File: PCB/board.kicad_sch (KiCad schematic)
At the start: 171 parts, among them J1 Micro_SD_Card, J10 Conn_01x10, J11 Conn_01x02, J12 Conn_02x04_Odd_Even, J13 Conn_01x02, J14 Conn_01x02, J15 Conn_01x03, J16 Conn_01x02, J17 Conn_01x05, J18 Conn_01x04, J19 Conn_01x04, J2 Conn_ARM_JTAG_SWD_10, J20 Conn_01x02, J21 Conn_01x03, J22 Conn_02x04_Odd_Even, J23 Conn_01x04, J24 Conn_01x04, J25 Conn_01x02, J26 Conn_01x03, J27 Conn_02x04_Odd_Even, J28 Conn_01x04, J29 Conn_01x04, J30 Conn_01x02, J31 Conn_01x03, J32 Conn_01x02, J33 Conn_01x02, J34 Conn_01x02, J35 Conn_01x02, J36 Conn_01x02, J37 Conn_01x02, J4 Conn_01x04, J5 Conn_01x04, J6 Conn_01x02, J7 Conn_01x03, J8 Conn_02x04_Odd_Even, J9 Conn_01x10, P1 USB_C_Plug_USB2.0, Q1 IRLML6402, Q2 NMOS, Q3 NMOS, Q4 NMOS, Q5 NMOS, Q6 NMOS, SW1 SW_SPST, SW2 SW_Push, U1 STM32H743VITx, U2 AMS1117-3.3, U3 TPS54331, U4 TMC2209_SILENTSTEPSTICK, U5 TMC2209_SILENTSTEPSTICK, U6 TMC2209_SILENTSTEPSTICK, U7 TMC2209_SILENTSTEPSTICK, Y1 25 MHz

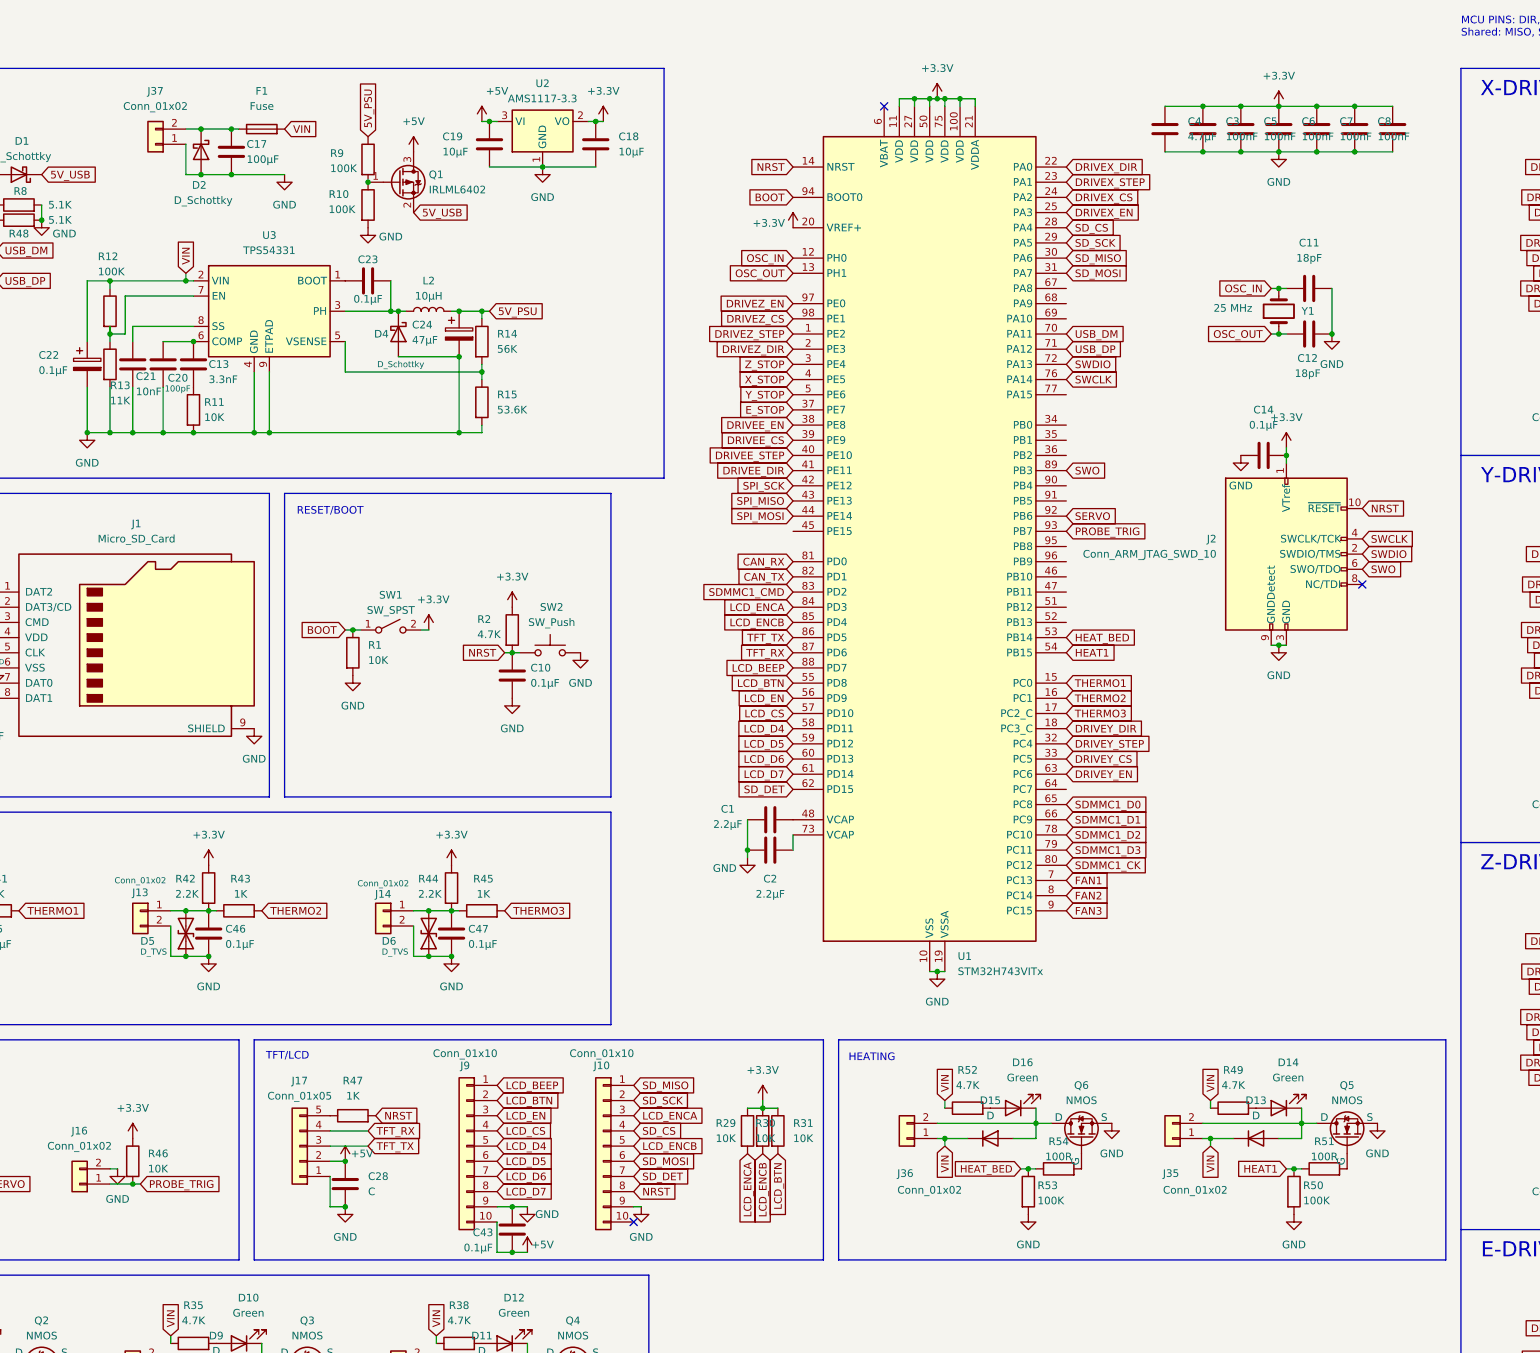
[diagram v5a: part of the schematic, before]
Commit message: most of the capacitors using assign footprints
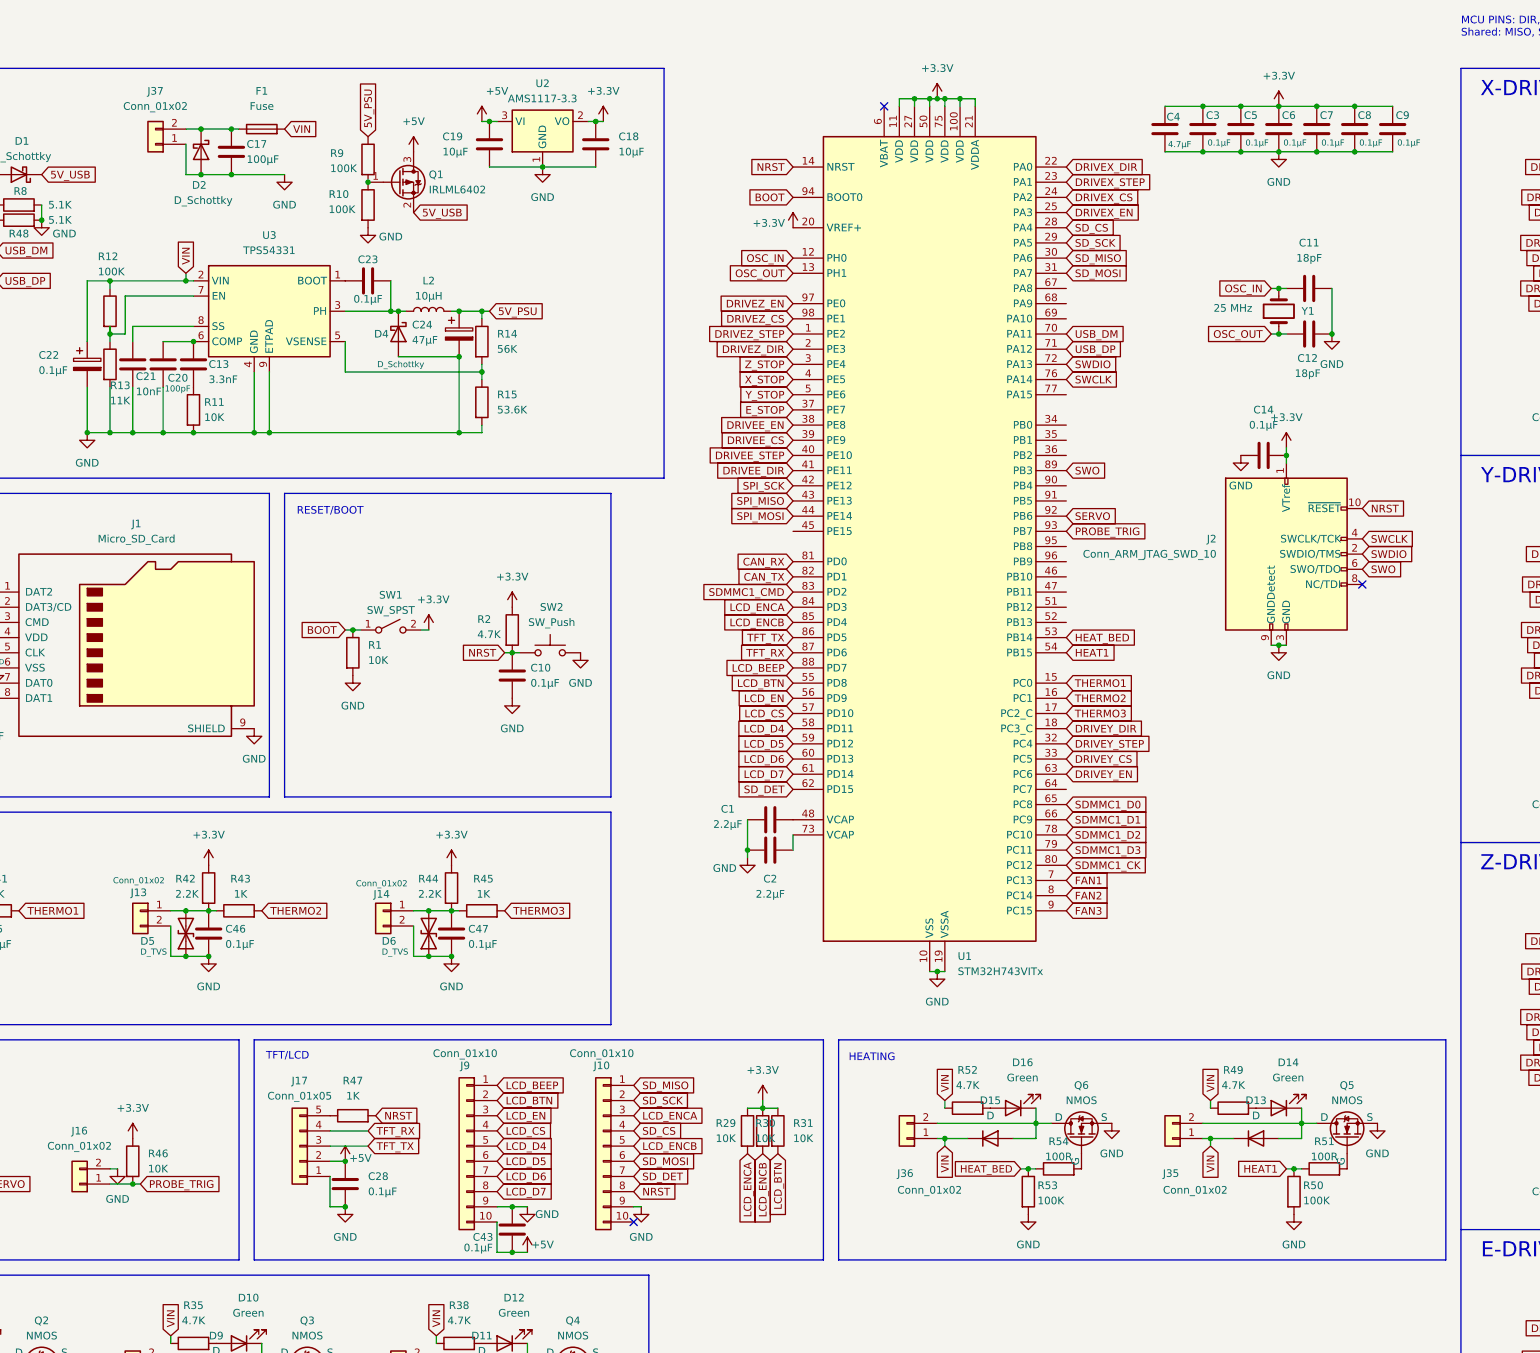
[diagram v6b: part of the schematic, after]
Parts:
- C1, C2, C4: footprint (none) -> Capacitor_SMD:C_0805_2012Metric
- C13, C21: footprint Capacitor_SMD:C_0603_1608Metric -> Capacitor_SMD:C_0805_2012Metric
- C28: value C -> 0.1µF
- C3, C5, C6, C7, C8, C9: value 100nF -> 0.1µF; footprint (none) -> Capacitor_SMD:C_0603_1608Metric

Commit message: some more footprints
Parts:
- C11, C12, C14, C27, C28, C29, C30, C32, C33, C34, C36, C37, C38, C40, C41, C42, C43, C49: footprint (none) -> Capacitor_SMD:C_0603_1608Metric
- C26, C31, C35, C39: footprint (none) -> Capacitor_SMD:CP_Elec_10x10.5
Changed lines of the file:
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@@
 			)
 		)
-		(property "Footprint" ""
+		(property "Footprint" "Capacitor_SMD:C_0603_1608Metric"
 			(at 362.9152 228.6 0)
 			(effects
@@
 			)
 		)
-		(property "Footprint" ""
+		(property "Footprint" "Capacitor_SMD:C_0603_1608Metric"
 			(at 362.9152 99.06 0)
 			(effects
@@
 			)
 		)
-		(property "Footprint" ""
+		(property "Footprint" "Capacitor_SMD:C_0603_1608Metric"
 			(at 375.6152 57.15 0)
 			(effects
@@
 			)
 		)
-		(property "Footprint" ""
+		(property "Footprint" "Capacitor_SMD:C_0603_1608Metric"
 			(at 375.6152 121.92 0)
 			(effects
@@
 			)
 		)
-		(property "Footprint" ""
+		(property "Footprint" "Capacitor_SMD:CP_Elec_10x10.5"
 			(at 350.2152 34.29 0)
 			(effects
@@
 			)
 		)
-		(property "Footprint" ""
+		(property "Footprint" "Capacitor_SMD:C_0603_1608Metric"
 			(at 355.2952 34.29 0)
 			(effects
@@
 			)
 		)
-		(property "Footprint" ""
+		(property "Footprint" "Capacitor_SMD:C_0603_1608Metric"
 			(at 130.5052 212.09 0)
 			(effects
@@
 			)
 		)
-		(property "Footprint" ""
+		(property "Footprint" "Capacitor_SMD:C_0603_1608Metric"
 			(at 355.2952 99.06 0)
 			(effects
@@
 			)
 		)
-		(property "Footprint" ""
+		(property "Footprint" "Capacitor_SMD:CP_Elec_10x10.5"
 			(at 350.2152 163.83 0)
 			(effects
@@
 			)
 		)
-		(property "Footprint" ""
+		(property "Footprint" "Capacitor_SMD:C_0603_1608Metric"
 			(at 355.2952 163.83 0)
 			(effects
@@
 			)
 		)
-		(property "Footprint" ""
+		(property "Footprint" "Capacitor_SMD:C_0603_1608Metric"
 			(at 375.6152 251.46 0)
 			(effects
@@
 			)
 		)
-		(property "Footprint" ""
+		(property "Footprint" "Capacitor_SMD:C_0603_1608Metric"
 			(at 33.9852 198.12 0)
 			(effects
@@
 			)
 		)
-		(property "Footprint" ""
+		(property "Footprint" "Capacitor_SMD:C_0603_1608Metric"
 			(at 355.2952 228.6 0)
 			(effects
@@
 			)
 		)
-		(property "Footprint" ""
+		(property "Footprint" "Capacitor_SMD:C_0603_1608Metric"
 			(at 362.9152 34.29 0)
 			(effects
@@
 			)
 		)
-		(property "Footprint" ""
+		(property "Footprint" "Capacitor_SMD:C_0603_1608Metric"
 			(at 102.5652 204.47 0)
 			(effects
@@
 			)
 		)
-		(property "Footprint" ""
+		(property "Footprint" "Capacitor_SMD:C_0603_1608Metric"
 			(at 266.7 57.4548 0)
 			(effects
@@
 			)
 		)
-		(property "Footprint" ""
+		(property "Footprint" "Capacitor_SMD:C_0603_1608Metric"
 			(at 266.7 49.8348 0)
 			(effects
@@
 			)
 		)
-		(property "Footprint" ""
+		(property "Footprint" "Capacitor_SMD:CP_Elec_10x10.5"
 			(at 350.2152 99.06 0)
 			(effects
@@
 			)
 		)
-		(property "Footprint" ""
+		(property "Footprint" "Capacitor_SMD:C_0603_1608Metric"
 			(at 259.08 77.7748 0)
 			(effects
@@
 			)
 		)
-		(property "Footprint" ""
+		(property "Footprint" "Capacitor_SMD:C_0603_1608Metric"
 			(at 362.9152 163.83 0)
 			(effects
@@
 			)
 		)
-		(property "Footprint" ""
+		(property "Footprint" "Capacitor_SMD:C_0603_1608Metric"
 			(at 375.6152 186.69 0)
 			(effects
@@
 			)
 		)
-		(property "Footprint" ""
+		(property "Footprint" "Capacitor_SMD:CP_Elec_10x10.5"
 			(at 350.2152 228.6 0)
 			(effects

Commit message: A LOT more footprint stuff
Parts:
- added C44: 0.1µF, Capacitor_SMD:C_0603_1608Metric, symbol Device:C
- D7, R16, R17, R18, R21, R23, R25, R26, R28, R29, R30, R31, R32, R33, R34, R35, R36, R37, R38, R39, R40, R46, R47, R49, R50, R51, R52, R53, R54: footprint (none) -> Resistor_SMD:R_0603_1608Metric
- R14, R15, R9: footprint Resistor_SMD:R_0603_1608Metric -> Resistor_SMD:R_0805_2012Metric
- R20, R22, R24, R27: footprint (none) -> Resistor_SMD:R_0805_2012Metric
- R48, R8: footprint Resistor_SMD:R_0402_1005Metric -> Resistor_SMD:R_0603_1608Metric
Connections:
- net 5V_USB: now also C44.1
- net GND: now also C44.2
